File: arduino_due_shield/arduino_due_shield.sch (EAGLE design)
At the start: 27 parts, among them J12 ARDUINO_MEGA_R3FULL, J13 POLOLU-2595, J14 POLOLU-2807, J15 POLOLU-2595

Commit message: Finish schematic and PCB design
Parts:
- removed R4: 3.3k, resistor:R-US_0204/7
- removed R5: 2.2k, resistor:R-US_0204/7
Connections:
- net RX1 renamed RC_RX1
- net RX2 renamed RC_RX2
- net RX3 renamed RC_RX3
- removed net RELAYHV: JP11.2, R4.2
- new net N$2: J14.FAILMODE1, J14.FAILMODE2
- new net RELAYOUT_HV: J13.H4, JP11.2
- net GND: no longer R5.1
- net RELAYOUT: now also J13.L4; no longer R4.1, R5.2
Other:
- note added: "Arduino Shield Outline"
- note added: "AutoRally Arduino Due Shield"
- note added: "Buzzer"
- note added: "Misc. Connectors"
- note added: "Multiplexer"
- note added: "PCB designed by Josh Oldenburg, fall 2019"
- note added: "RC receiver"
- note removed: "Jumper intentionally not connected"
- moved on the sheet: C1, C2, C3, C4, C5, J12, J13, J14, J15, JP1, JP10, JP11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

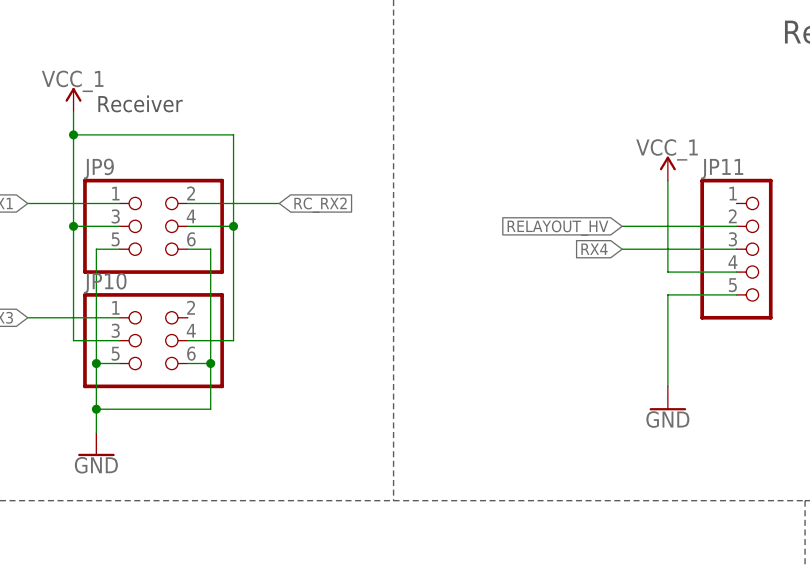
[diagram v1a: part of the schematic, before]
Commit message: Add missing RC_RX4 net
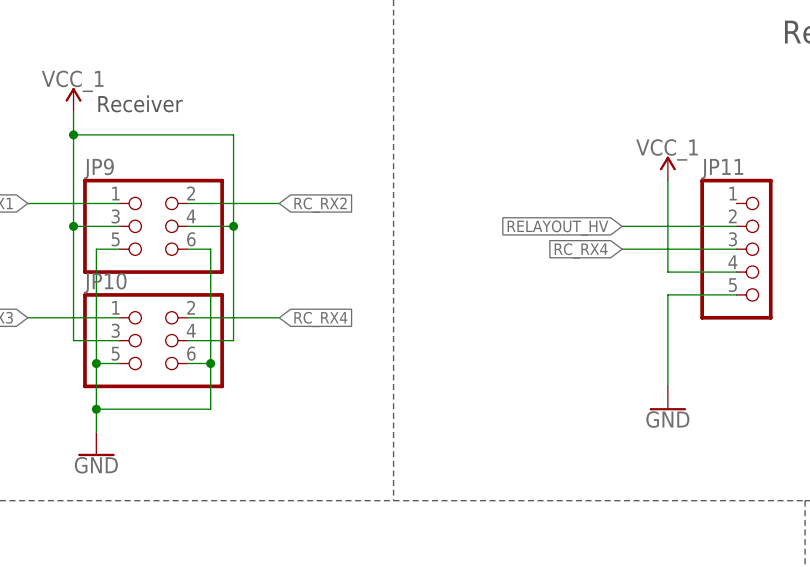
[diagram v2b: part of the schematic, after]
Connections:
- removed net RX4: JP11.3
- new net RC_RX4: JP10.2, JP11.3
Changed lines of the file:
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@@
 </segment>
 </net>
-<net name="RX4" class="0">
+<net name="RC_RX4" class="0">
 <segment>
 <pinref part="JP11" gate="A" pin="3"/>
@@
 <label x="83.82" y="177.8" size="1.27" layer="95" rot="R180" xref="yes"/>
 </segment>
+<segment>
+<pinref part="JP10" gate="A" pin="2"/>
+<wire x1="35.56" y1="170.18" x2="45.72" y2="170.18" width="0.1524" layer="91"/>
+<label x="45.72" y="170.18" size="1.27" layer="95" xref="yes"/>
+</segment>
 </net>
